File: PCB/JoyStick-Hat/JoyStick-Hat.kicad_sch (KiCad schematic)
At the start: 0 parts

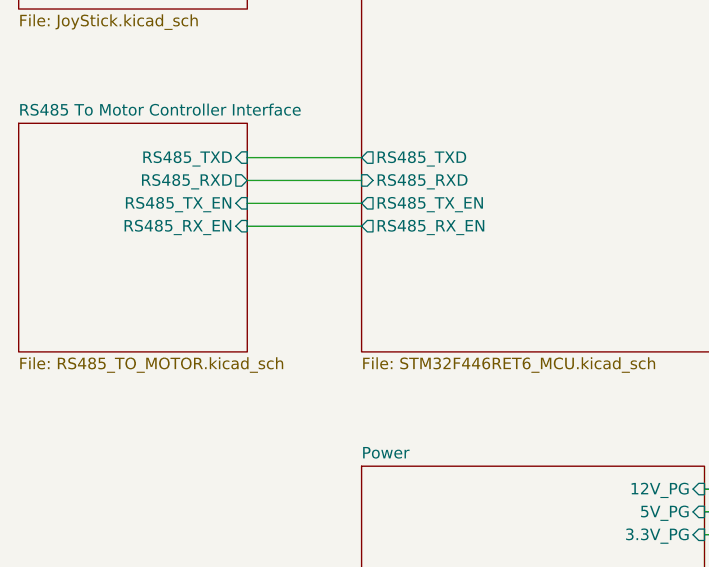
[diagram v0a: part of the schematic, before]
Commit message: RJ45
Replaced RJ45 connector, original one had magnetics, those are not needed for RS485 and would have caused problems. Hooked up coms LEDs on RJ45 connector to MCU for debugging and displaying coms activity.
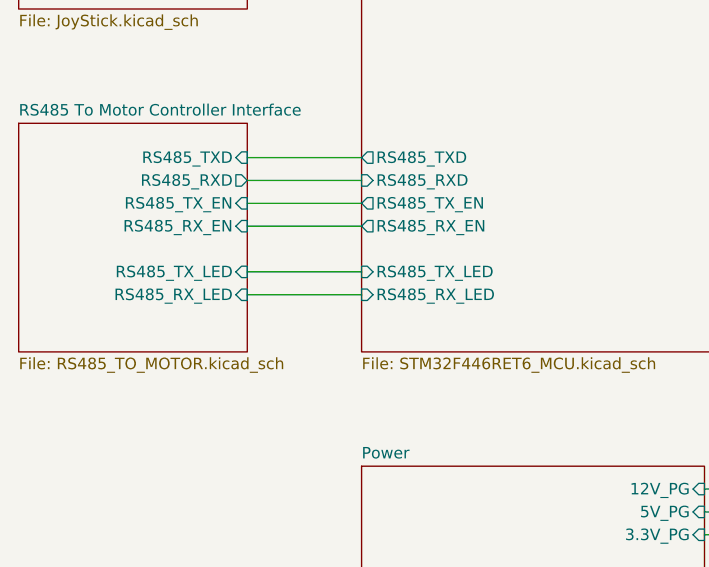
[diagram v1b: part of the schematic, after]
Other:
- sheet RS485 To Motor Controller Interface ports: added RS485_RX_LED, RS485_TX_LED; removed none
- sheet STM32F446RET6-MCU ports: added RS485_RX_LED, RS485_TX_LED; removed none
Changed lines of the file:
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@@
+	(wire
+		(pts
+			(xy 101.6 133.35) (xy 114.3 133.35)
+		)
+		(stroke
+			(width 0)
+			(type default)
+		)
+	)
 	(wire
 		(pts
@@
 		(pts
 			(xy 101.6 120.65) (xy 114.3 120.65)
+		)
+		(stroke
+			(width 0)
+			(type default)
+		)
+	)
+	(wire
+		(pts
+			(xy 101.6 130.81) (xy 114.3 130.81)
 		)
 		(stroke
@@
 			)
 		)
+		(pin "RS485_TX_LED" input
+			(at 101.6 130.81 0)
+			(effects
+				(font
+					(size 1.27 1.27)
+				)
+				(justify right)
+			)
+		)
+		(pin "RS485_RX_LED" input
+			(at 101.6 133.35 0)
+			(effects
+				(font
+					(size 1.27 1.27)
+				)
+				(justify right)
+			)
+		)
 		(instances
 			(project "JoyStick-Hat"
@@
 			(effects
 				(font
+					(size 1.27 1.27)
+				)
+				(justify left)
+			)
+		)
+		(pin "RS485_TX_LED" input
+			(at 114.3 130.81 180)
+			(effects
+				(font
+					(size 1.27 1.27)
+				)
+				(justify left)
+			)
+		)
+		(pin "RS485_RX_LED" input
+			(at 114.3 133.35 180)
+			(effects
+				(font
